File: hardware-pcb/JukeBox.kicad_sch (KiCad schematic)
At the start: 79 parts, among them J1 USB4105-GF-A, J2 Conn_01x04_Pin, Q1 Q_NPN_BEC, SW1 SW_SPST, SW10 SW_SPST, SW11 SW_SPST, SW12 SW_SPST, SW2 SW_SPST, SW3 SW_SPST, SW4 SW_SPST, SW5 SW_SPST, SW6 SW_SPST, SW7 SW_SPST, SW8 SW_SPST, SW9 SW_SPST, U1 NCP1117-3.3_SOT223, U2 W25Q16JVUXIQ TR, U3 RP2040, U4 st7789v, Y1 ECS-120-20-33-AEL-TR

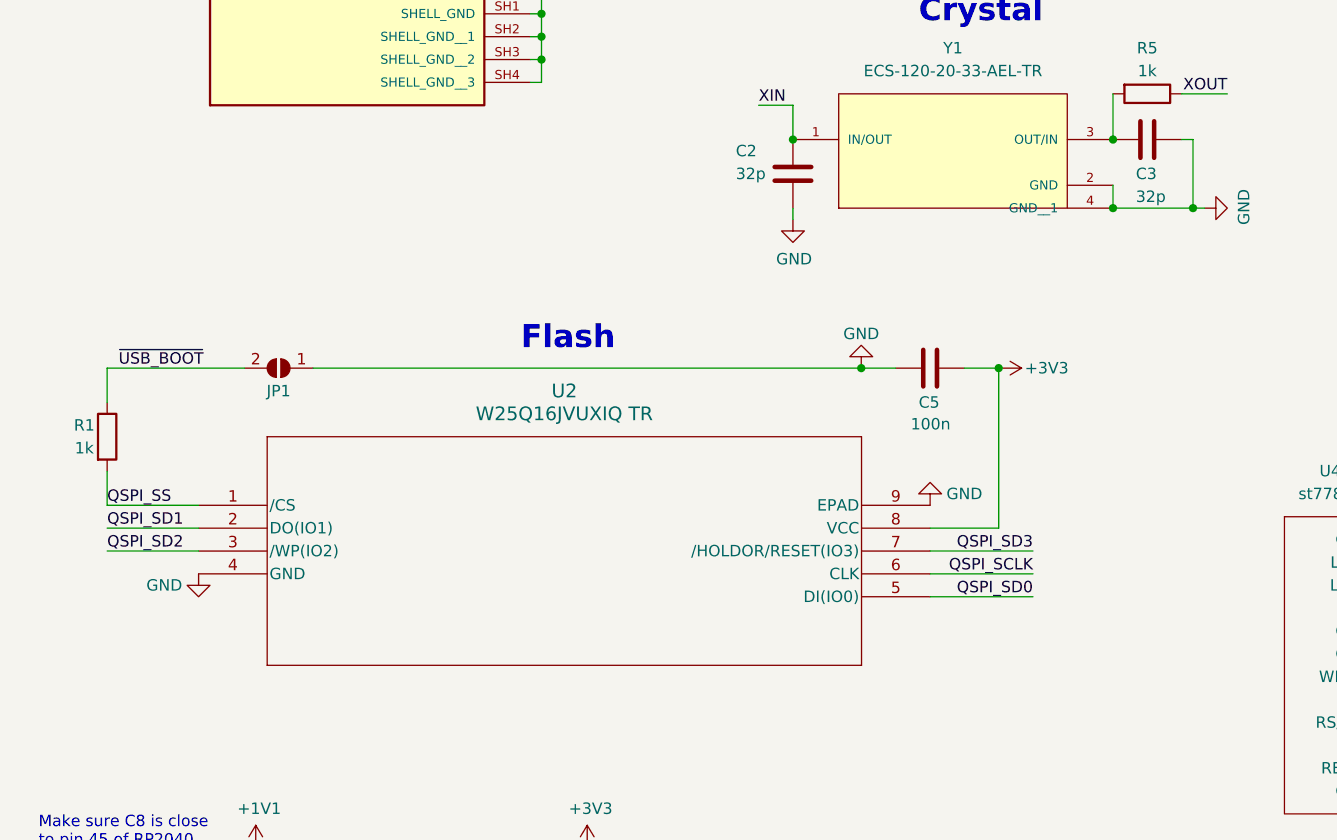
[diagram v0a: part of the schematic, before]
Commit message: remove old cad files, switch to 8MB flash
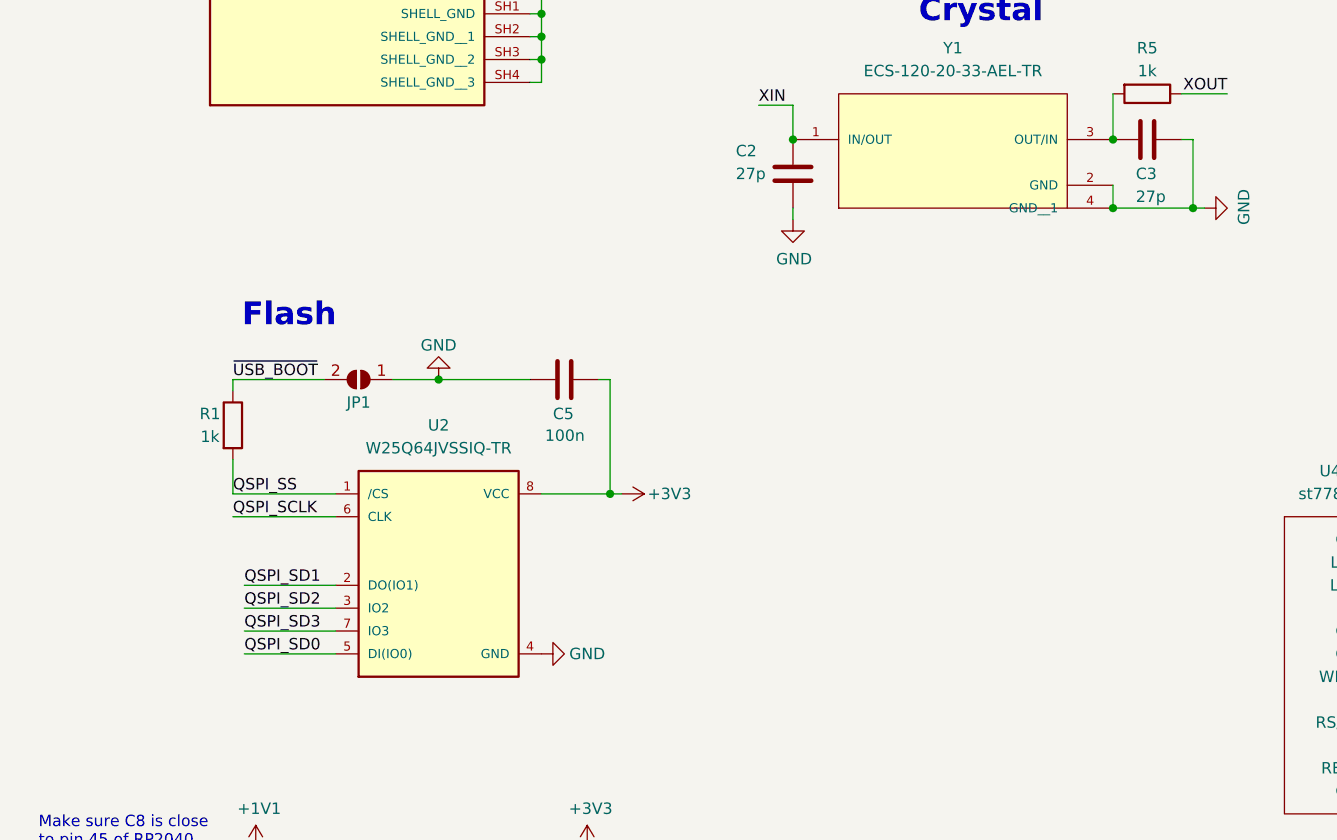
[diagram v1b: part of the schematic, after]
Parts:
- removed U2: W25Q16JVUXIQ TR, JukeBox:USON-8_UX_2x3x0p6_WIN, symbol W25Q16JVUXIQ-TR:W25Q16JVUXIQ_TR
- added U2: W25Q64JVSSIQ-TR, Package_SO:SOIC-8W_5.3x5.3mm_P1.27mm, symbol W25Q64JVZPIQ-TR:W25Q64JVZPIQ-TR
- C2, C3: value 32p -> 27p
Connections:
- net +3V3: now also U2.8 (VCC)
- net GND: now also U2.4 (GND)
- net QSPI_SCLK: now also U2.6 (CLK)
- net QSPI_SD0: now also U2.5 (DI(IO0))
- net QSPI_SD1: now also U2.2 (DO(IO1))
- net QSPI_SD2: now also U2.3 (IO2)
- net QSPI_SD3: now also U2.7 (IO3)
- net QSPI_SS: now also U2.1 (/CS)
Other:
- moved on the sheet: C5, JP1, R1

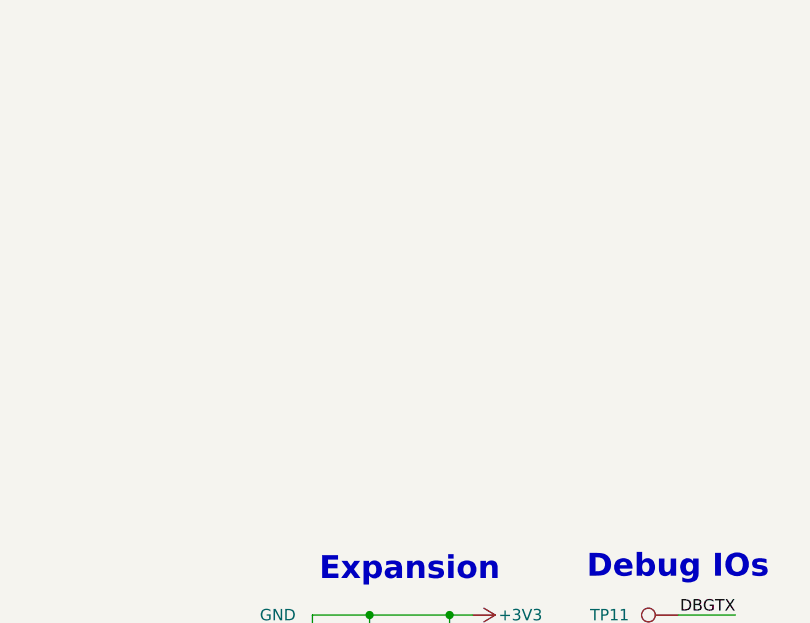
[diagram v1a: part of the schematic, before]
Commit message: add eeprom for configuring the device persistently
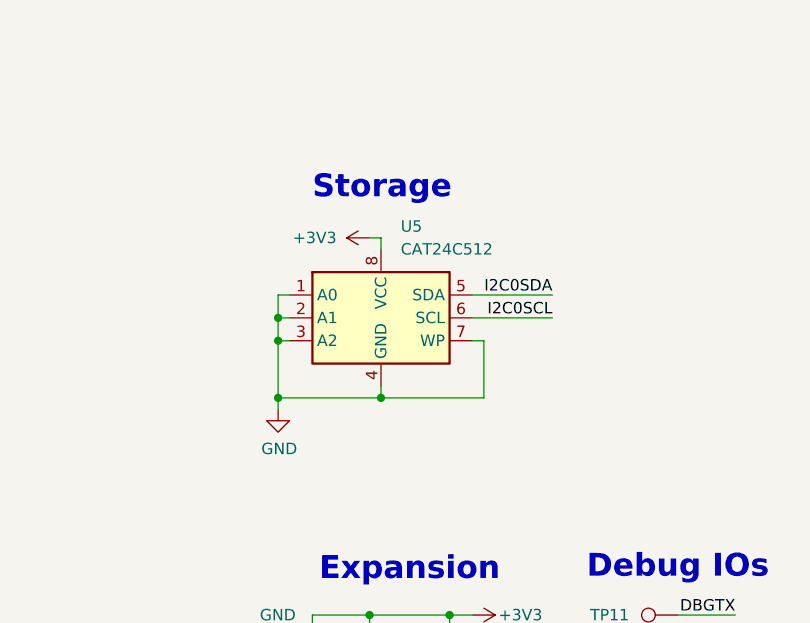
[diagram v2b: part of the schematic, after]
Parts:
- added U5: CAT24C512, Package_SO:SOIC-8_3.9x4.9mm_P1.27mm, symbol Memory_EEPROM:CAT24C128
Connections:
- net +3V3: now also U5.8 (VCC)
- net GND: now also U5.1 (A0), U5.2 (A1), U5.3 (A2), U5.4 (GND), U5.7 (WP)
- net GPIO4: now also U5.5 (SDA)
- net GPIO5: now also U5.6 (SCL)
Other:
- note added: "Storage"

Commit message: switch to internal kicad usb c, switch to pico clock, fix clock capacitance, fix rgb pinout, fix missing BOM materials
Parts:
- removed D13, D14, D15, D16, D17, D18, D19, D20, D21, D22, D23, D24: WS2812B, LED_SMD:LED_WS2812B-2020_PLCC4_2.0x2.0mm, symbol LED:WS2812B
- removed J1: USB4105-GF-A, JukeBox:GCT_USB4105-GF-A, symbol USB4105-GF-A:USB4105-GF-A
- removed Y1: ECS-120-20-33-AEL-TR, JukeBox:XTAL_ECS-120-20-33-AEL-TR, symbol ECS-120-20-33-AEL-TR:ECS-120-20-33-AEL-TR
- added D13, D14, D15, D16, D17, D18, D19, D20, D21, D22, D23, D24: WS2812B, LED_SMD:LED_WS2812B-2020_PLCC4_2.0x2.0mm, symbol LED:WS2812B-2020
- added J1: USB_C_Receptacle_USB2.0_16P, Connector_USB:USB_C_Receptacle_GCT_USB4105-xx-A_16P_TopMnt_Horizontal, symbol Connector:USB_C_Receptacle_USB2.0_16P
- added Y2: ABM8-272-T3, Crystal:Crystal_SMD_Abracon_ABM8G-4Pin_3.2x2.5mm, symbol Device:Crystal_GND24
- C2, C3: value 27p -> 15p
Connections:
- net GND: now also C2.1, C3.2, D13.2 (VSS), D14.2 (VSS), D15.2 (VSS), D16.2 (VSS), D17.2 (VSS), D18.2 (VSS), D19.2 (VSS), D20.2 (VSS), D21.2 (VSS), D22.2 (VSS), D23.2 (VSS), D24.2 (VSS), J1.A1 (GND), J1.A12 (GND), J1.B1 (GND), J1.B12 (GND), J1.S1 (SHIELD), Y2.2, Y2.4; no longer C2.2, C3.1
- net GPIO2: now also D13.3 (DIN)
- net RGBDOUT: now also D24.1 (DOUT)
- net USB_D+: now also J1.A6 (D+), J1.B6 (D+)
- net USB_D-: now also J1.A7 (D-), J1.B7 (D-)
- net VBUS: now also D13.4 (VDD), D14.4 (VDD), D15.4 (VDD), D16.4 (VDD), D17.4 (VDD), D18.4 (VDD), D19.4 (VDD), D20.4 (VDD), D21.4 (VDD), D22.4 (VDD), D23.4 (VDD), D24.4 (VDD), J1.A4 (VBUS), J1.A9 (VBUS), J1.B4 (VBUS), J1.B9 (VBUS)
- net XIN: now also C3.1, Y2.1; no longer C2.1
- net at R5.2: now also C2.2, Y2.3; no longer C3.2
- net at R7.1: now also J1.B5 (CC2)
- net at R6.1: now also J1.A5 (CC1)
- new net: D23.1 (DOUT), D24.3 (DIN)
- new net: D22.1 (DOUT), D23.3 (DIN)
- new net: D16.1 (DOUT), D17.3 (DIN)
- new net: D15.1 (DOUT), D16.3 (DIN)
- new net: D18.1 (DOUT), D19.3 (DIN)
- new net: D17.1 (DOUT), D18.3 (DIN)
- new net: D14.1 (DOUT), D15.3 (DIN)
- new net: D19.1 (DOUT), D20.3 (DIN)
- new net: D21.1 (DOUT), D22.3 (DIN)
- new net: D20.1 (DOUT), D21.3 (DIN)
- new net: D13.1 (DOUT), D14.3 (DIN)
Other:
- moved on the sheet: C2, C3, R5, R6, R7

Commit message: switch from 0805 to 0402
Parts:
- C1, C10, C2, C3, C4, C5, C8: footprint Capacitor_SMD:C_0805_2012Metric_Pad1.18x1.45mm_HandSolder -> Capacitor_SMD:C_0402_1005Metric
- R1, R10, R11, R12, R13, R14, R15, R21, R22, R3, R4, R5, R6, R7, R8, R9: footprint Resistor_SMD:R_0805_2012Metric_Pad1.20x1.40mm_HandSolder -> Resistor_SMD:R_0402_1005Metric
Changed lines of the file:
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@@
 			)
 		)
-		(property "Footprint" "Capacitor_SMD:C_0805_2012Metric_Pad1.18x1.45mm_HandSolder"
+		(property "Footprint" "Capacitor_SMD:C_0402_1005Metric"
 			(at 110.49 77.7748 0)
 			(effects
@@
 			)
 		)
-		(property "Footprint" "Capacitor_SMD:C_0805_2012Metric_Pad1.18x1.45mm_HandSolder"
+		(property "Footprint" "Capacitor_SMD:C_0402_1005Metric"
 			(at 102.87 69.5452 0)
 			(effects
@@
 			)
 		)
-		(property "Footprint" "Capacitor_SMD:C_0805_2012Metric_Pad1.18x1.45mm_HandSolder"
+		(property "Footprint" "Capacitor_SMD:C_0402_1005Metric"
 			(at 69.85 101.2952 0)
 			(effects
@@
 			)
 		)
-		(property "Footprint" "Capacitor_SMD:C_0805_2012Metric_Pad1.18x1.45mm_HandSolder"
+		(property "Footprint" "Capacitor_SMD:C_0402_1005Metric"
 			(at 31.4452 163.83 0)
 			(effects
@@
 			)
 		)
-		(property "Footprint" "Capacitor_SMD:C_0805_2012Metric_Pad1.18x1.45mm_HandSolder"
+		(property "Footprint" "Capacitor_SMD:C_0402_1005Metric"
 			(at 83.5152 163.83 0)
 			(effects
@@
 			)
 		)
-		(property "Footprint" "Capacitor_SMD:C_0805_2012Metric_Pad1.18x1.45mm_HandSolder"
+		(property "Footprint" "Capacitor_SMD:C_0402_1005Metric"
 			(at 97.4852 40.64 0)
 			(effects
@@
 			)
 		)
-		(property "Footprint" "Capacitor_SMD:C_0805_2012Metric_Pad1.18x1.45mm_HandSolder"
+		(property "Footprint" "Capacitor_SMD:C_0402_1005Metric"
 			(at 122.8852 40.64 0)
 			(effects
@@
 			)
 		)
-		(property "Footprint" "Resistor_SMD:R_0805_2012Metric_Pad1.20x1.40mm_HandSolder"
+		(property "Footprint" "Resistor_SMD:R_0402_1005Metric"
 			(at 132.08 76.962 90)
 			(effects
@@
 			)
 		)
-		(property "Footprint" "Resistor_SMD:R_0805_2012Metric_Pad1.20x1.40mm_HandSolder"
+		(property "Footprint" "Resistor_SMD:R_0402_1005Metric"
 			(at 73.66 50.038 90)
 			(effects
@@
 			)
 		)
-		(property "Footprint" "Resistor_SMD:R_0805_2012Metric_Pad1.20x1.40mm_HandSolder"
+		(property "Footprint" "Resistor_SMD:R_0402_1005Metric"
 			(at 379.222 204.47 90)
 			(effects
@@
 			)
 		)
-		(property "Footprint" "Resistor_SMD:R_0805_2012Metric_Pad1.20x1.40mm_HandSolder"
+		(property "Footprint" "Resistor_SMD:R_0402_1005Metric"
 			(at 111.76 181.102 90)
 			(effects
@@
 			)
 		)
-		(property "Footprint" "Resistor_SMD:R_0805_2012Metric_Pad1.20x1.40mm_HandSolder"
+		(property "Footprint" "Resistor_SMD:R_0402_1005Metric"
 			(at 358.902 204.47 90)
 			(effects
@@
 			)
 		)
-		(property "Footprint" "Resistor_SMD:R_0805_2012Metric_Pad1.20x1.40mm_HandSolder"
+		(property "Footprint" "Resistor_SMD:R_0402_1005Metric"
 			(at 73.66 42.418 90)
 			(effects
@@
 			)
 		)
-		(property "Footprint" "Resistor_SMD:R_0805_2012Metric_Pad1.20x1.40mm_HandSolder"
+		(property "Footprint" "Resistor_SMD:R_0402_1005Metric"
 			(at 111.76 173.482 90)
 			(effects
@@
 			)
 		)
-		(property "Footprint" "Resistor_SMD:R_0805_2012Metric_Pad1.20x1.40mm_HandSolder"
+		(property "Footprint" "Resistor_SMD:R_0402_1005Metric"
 			(at 399.542 204.47 90)
 			(effects
@@
 			)
 		)
-		(property "Footprint" "Resistor_SMD:R_0805_2012Metric_Pad1.20x1.40mm_HandSolder"
+		(property "Footprint" "Resistor_SMD:R_0402_1005Metric"
 			(at 220.98 121.158 90)
 			(effects
@@
 			)
 		)
-		(property "Footprint" "Resistor_SMD:R_0805_2012Metric_Pad1.20x1.40mm_HandSolder"
+		(property "Footprint" "Resistor_SMD:R_0402_1005Metric"
 			(at 199.39 124.968 90)
 			(effects
@@
 			)
 		)
-		(property "Footprint" "Resistor_SMD:R_0805_2012Metric_Pad1.20x1.40mm_HandSolder"
+		(property "Footprint" "Resistor_SMD:R_0402_1005Metric"
 			(at 338.582 204.47 90)
 			(effects
@@
 			)
 		)
-		(property "Footprint" "Resistor_SMD:R_0805_2012Metric_Pad1.20x1.40mm_HandSolder"
+		(property "Footprint" "Resistor_SMD:R_0402_1005Metric"
 			(at 199.39 133.858 90)
 			(effects
@@
 			)
 		)
-		(property "Footprint" "Resistor_SMD:R_0805_2012Metric_Pad1.20x1.40mm_HandSolder"
+		(property "Footprint" "Resistor_SMD:R_0402_1005Metric"
 			(at 190.5 70.612 90)
 			(effects
@@
 			)
 		)
-		(property "Footprint" "Resistor_SMD:R_0805_2012Metric_Pad1.20x1.40mm_HandSolder"
+		(property "Footprint" "Resistor_SMD:R_0402_1005Metric"
 			(at 160.782 264.16 90)
 			(effects
@@
 			)
 		)
-		(property "Footprint" "Resistor_SMD:R_0805_2012Metric_Pad1.20x1.40mm_HandSolder"
+		(property "Footprint" "Resistor_SMD:R_0402_1005Metric"
 			(at 35.052 105.41 90)
 			(effects
@@
 			)
 		)
-		(property "Footprint" "Resistor_SMD:R_0805_2012Metric_Pad1.20x1.40mm_HandSolder"
+		(property "Footprint" "Resistor_SMD:R_0402_1005Metric"
 			(at 169.672 264.16 90)
 			(effects
